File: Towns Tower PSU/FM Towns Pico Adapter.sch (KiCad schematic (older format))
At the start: 5 parts, among them J1 ATX24RH, J2 PCN13-44S-2.54DS_71_, U1 ProMicro

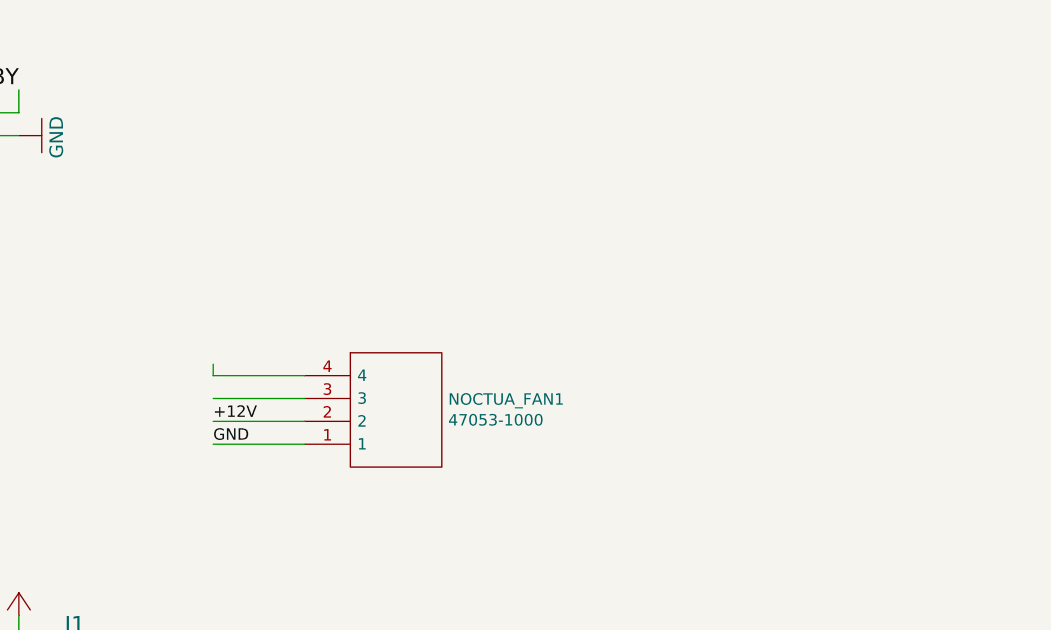
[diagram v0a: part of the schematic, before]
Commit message: TownsPSU Rev3
-SLG62686 footprint added. Will add configuration file once verified on hardware although I don't see anyone using them.
-Moved fan connector since someone complained
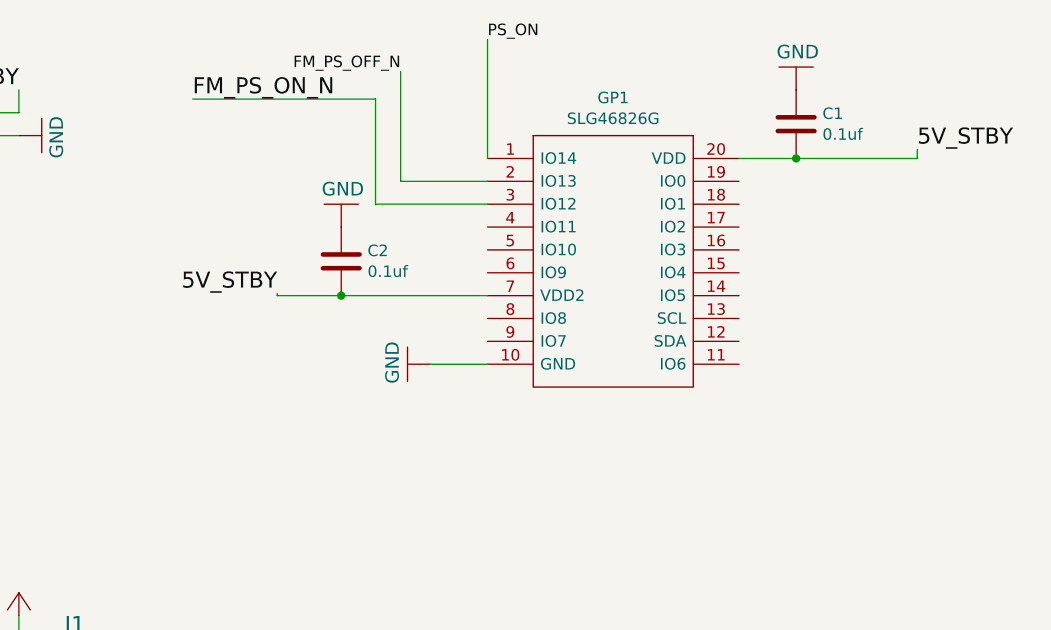
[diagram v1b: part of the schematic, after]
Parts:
- removed NOCTUA_FAN1: 47053-1000, Connector:FanPinHeader_1x04_P2.54mm_Vertical, symbol Imported_Parts:47053-1000
- added C1, C2: 0.1uf, Capacitor_SMD:C_1206_3216Metric, symbol Device:C
- added GP1: SLG46826G, SamacSys_Parts:SOP65P640X120-20N, symbol SamacSys_Parts:SLG46826G
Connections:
- net 5V_STBY: now also C1.2, C2.2, GP1.20 (VDD), GP1.7 (VDD2)
- net FM_PS_OFF_N: now also GP1.2 (IO13)
- net FM_PS_ON_N: now also GP1.3 (IO12)
- net PS_ON: now also GP1.1 (IO14)
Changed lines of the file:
@@
 	3350 2800 4150 2800
 $Comp
-L Imported_Parts:47053-1000 NOCTUA_FAN1
-U 1 1 607D9E9B
-P 7050 3150
-F 0 "NOCTUA_FAN1" H 7678 3046 50  0000 L CNN
-F 1 "47053-1000" H 7678 2955 50  0000 L CNN
-F 2 "Connector:FanPinHeader_1x04_P2.54mm_Vertical" H 7700 3250 50  0001 L CNN
-F 3 "http://www.molex.com/pdm_docs/sd/470531000_sd.pdf" H 7700 3150 50  0001 L CNN
-F 4 "MOLEX - 47053-1000 - HEADER, 4POS, 1ROW, 2.54MM" H 7700 3050 50  0001 L CNN "Description"
-F 5 "8" H 7700 2950 50  0001 L CNN "Height"
-F 6 "Molex" H 7700 2850 50  0001 L CNN "Manufacturer_Name"
-F 7 "47053-1000" H 7700 2750 50  0001 L CNN "Manufacturer_Part_Number"
-F 8 "538-47053-1000" H 7700 2650 50  0001 L CNN "Mouser Part Number"
-F 9 "https://www.mouser.co.uk/ProductDetail/Molex/47053-1000/?qs=ph4zPCVRuvqoDX7hrEhxNA%3D%3D" H 7700 2550 50  0001 L CNN "Mouser Price/Stock"
-F 10 "" H 7700 2450 50  0001 L CNN "Arrow Part Number"
-F 11 "" H 7700 2350 50  0001 L CNN "Arrow Price/Stock"
-	1    7050 3150
+L SamacSys_Parts:SLG46826G GP1
+U 1 1 648C70A9
+P 7850 2200
+F 0 "GP1" H 8400 2465 50  0000 C CNN
+F 1 "SLG46826G" H 8400 2374 50  0000 C CNN
+F 2 "SamacSys_Parts:SOP65P640X120-20N" H 8800 2300 50  0001 L CNN
+F 3 "https://www.renesas.com/us/en/products/programmable-mixed-signal-asic-ip-products/greenpak-programmable-mixed-signal-products/greenpak-system-programmability/slg46826-greenpak-programmable-mixed-signal-matrix-system-programmability" H 8800 2200 50  0001 L CNN
+F 4 "The SLG46826 provides a small, low power component for commonly used mixed-signal functions. The user creates the circuit design by programming the multiple time Non-Volatile Memory (NVM) to configure the interconnect logic, the IOs and the macrocells of the SLG46826. This highly versatile device allows a wide variety of mixed-signal functions to be designed within a very small, low power single integrated circuit.This product is available in both the Dual Supply GreenPAK and GreenPAK with In-System P" H 8800 2100 50  0001 L CNN "Description"
+F 5 "1.2" H 8800 2000 50  0001 L CNN "Height"
+F 6 "Renesas Electronics" H 8800 1900 50  0001 L CNN "Manufacturer_Name"
+F 7 "SLG46826G" H 8800 1800 50  0001 L CNN "Manufacturer_Part_Number"
+F 8 "724-SLG46826G" H 8800 1700 50  0001 L CNN "Mouser Part Number"
+F 9 "https://www.mouser.co.uk/ProductDetail/Renesas-Dialog/SLG46826G?qs=%252B6g0mu59x7Lz4SMy5idICg%3D%3D" H 8800 1600 50  0001 L CNN "Mouser Price/Stock"
+F 10 "" H 8800 1500 50  0001 L CNN "Arrow Part Number"
+F 11 "" H 8800 1400 50  0001 L CNN "Arrow Price/Stock"
+	1    7850 2200
 	1    0    0    -1
 $EndComp
 Wire Wire Line
-	7050 3150 6650 3150
+	7850 3100 7600 3100
+$Comp
+L FM_Towns_Pico_Adapter-eagle-import:GND #GND0103
+U 1 1 648C83CB
+P 7500 3100
+F 0 "#GND0103" H 7500 3100 50  0001 C CNN
+F 1 "GND" H 7400 3000 59  0000 L BNN
+F 2 "" H 7500 3100 50  0001 C CNN
+F 3 "" H 7500 3100 50  0001 C CNN
+	1    7500 3100
+	0    1    1    0
+$EndComp
 Wire Wire Line
-	6650 3150 6650 3100
+	8950 2200 9200 2200
+Text Label 9730 2160 0    70   ~ 0
+5V_STBY
+Text Label 6930 2790 2    70   ~ 0
+5V_STBY
+$Comp
+L Device:C C1
+U 1 1 648E94D3
+P 9200 2050
+F 0 "C1" H 9315 2096 50  0000 L CNN
+F 1 "0.1uf" H 9315 2005 50  0000 L CNN
+F 2 "Capacitor_SMD:C_1206_3216Metric" H 9238 1900 50  0001 C CNN
+F 3 "~" H 9200 2050 50  0001 C CNN
+	1    9200 2050
+	1    0    0    -1
+$EndComp
 Wire Wire Line
-	7050 3450 6650 3450
+	9200 2200 9730 2200
 Wire Wire Line
-	7050 3350 6650 3350
+	9730 2200 9730 2160
+Connection ~ 9200 2200
+$Comp
+L FM_Towns_Pico_Adapter-eagle-import:GND #GND0104
+U 1 1 648FD4E0
+P 9200 1800
+F 0 "#GND0104" H 9200 1800 50  0001 C CNN
+F 1 "GND" H 9100 1700 59  0000 L BNN
+F 2 "" H 9200 1800 50  0001 C CNN
+F 3 "" H 9200 1800 50  0001 C CNN
+	1    9200 1800
+	-1   0    0    1
+$EndComp
+$Comp
+L FM_Towns_Pico_Adapter-eagle-import:GND #GND0105
+U 1 1 64903BFF
+P 7210 2400
+F 0 "#GND0105" H 7210 2400 50  0001 C CNN
+F 1 "GND" H 7110 2300 59  0000 L BNN
+F 2 "" H 7210 2400 50  0001 C CNN
+F 3 "" H 7210 2400 50  0001 C CNN
+	1    7210 2400
+	-1   0    0    1
+$EndComp
+$Comp
+L Device:C C2
+U 1 1 64903BF9
+P 7210 2650
+F 0 "C2" H 7325 2696 50  0000 L CNN
+F 1 "0.1uf" H 7325 2605 50  0000 L CNN
+F 2 "Capacitor_SMD:C_1206_3216Metric" H 7248 2500 50  0001 C CNN
+F 3 "~" H 7210 2650 50  0001 C CNN
+	1    7210 2650
+	1    0    0    -1
+$EndComp
 Wire Wire Line
-	7050 3250 6650 3250
-Text Label 6650 3450 0    50   ~ 0
-GND
-Text Label 6650 3350 0    50   ~ 0
-+12V
+	7210 2800 7850 2800
+Wire Wire Line
+	7210 2800 6930 2800
+Wire Wire Line
+	6930 2800 6930 2790
+Connection ~ 7210 2800
+Wire Wire Line
+	7850 2200 7850 1680
+Wire Wire Line
+	7850 2300 7470 2300
+Wire Wire Line
+	7470 1820 7470 2300
+Wire Wire Line
+	7850 2400 7360 2400
+Wire Wire Line
+	7360 2400 7360 1940
+Text Label 6560 1940 0    70   ~ 0
+FM_PS_ON_N
+Wire Wire Line
+	6560 1940 7360 1940
+Text Label 7850 1680 0    50   ~ 0
+PS_ON
+Text Label 7470 1820 2    50   ~ 0
+FM_PS_OFF_N
 $EndSCHEMATC
